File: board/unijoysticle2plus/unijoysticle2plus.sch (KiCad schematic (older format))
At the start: 43 parts, among them J1 DB9_Female, J2 DB9_Female, J3 USB_B_Micro, Q1 S8050, Q2 S8050, SW1 RESET, SW2 JOY SWAP, U1 74HC05, U2 74HC05, U3 74HC05, U4 ESP32-WROOM-32D, U5 AMS1117-3.3, U6 CH340C

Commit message: unijoysticle2plus: no idea
Unfortunately I have no idea what these changes are.
I would guess it is "safe" to commit them.
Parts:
- removed H1, H2: MountingHole_Pad, MountingHole:MountingHole_3.2mm_M3_Pad_Via, symbol Mechanical:MountingHole_Pad
- R2, R3, R4: value 300 -> 1k; LCSC C17617 -> C17513
- renumbered H3 to H1, H4 to H2
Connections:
- wire segments 189 -> 187
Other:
- moved on the sheet: H1, H2
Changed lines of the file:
@@
 	3050 450  3050 3950
-Wire Notes Line
-	6850 4750 6800 4750
 Wire Notes Line
 	3700 5500 11050 5500
@@
 P 6550 5750
 F 0 "R2" V 6620 5750 50  0000 C CNN
-F 1 "300" V 6460 5750 50  0000 C CNN
+F 1 "1k" V 6460 5750 50  0000 C CNN
 F 2 "Resistor_SMD:R_0805_2012Metric_Pad1.20x1.40mm_HandSolder" V 6480 5750 50  0001 C CNN
 F 3 "~" H 6550 5750 50  0001 C CNN
-F 4 "C17617" V 6550 5750 50  0001 C CNN "LCSC"
+F 4 "C17513" V 6550 5750 50  0001 C CNN "LCSC"
 	1    6550 5750
 	0    -1   -1   0
@@
 NoConn ~ 9460 6110
 $Comp
-L Mechanical:MountingHole_Pad H3
-U 1 1 60D40B18
-P 8300 5830
-F 0 "H3" H 8250 6000 50  0000 L CNN
-F 1 "MountingHole_Pad" H 7960 5650 50  0001 L CNN
-F 2 "MountingHole:MountingHole_3.2mm_M3_Pad_Via" H 8300 5830 50  0001 C CNN
-F 3 "~" H 8300 5830 50  0001 C CNN
-	1    8300 5830
-	1    0    0    -1
-$EndComp
-$Comp
-L Mechanical:MountingHole_Pad H4
-U 1 1 60D4139A
-P 8550 5830
-F 0 "H4" H 8500 6000 50  0000 L CNN
-F 1 "MountingHole_Pad" H 8200 5650 50  0001 L CNN
-F 2 "MountingHole:MountingHole_3.2mm_M3_Pad_Via" H 8550 5830 50  0001 C CNN
-F 3 "~" H 8550 5830 50  0001 C CNN
-	1    8550 5830
-	1    0    0    -1
-$EndComp
-$Comp
 L Graphic:Logo_Open_Hardware_Small #LOGO1
 U 1 1 60C7EEFF
@@
 P 6550 6000
 F 0 "R3" V 6620 6000 50  0000 C CNN
-F 1 "300" V 6460 6000 50  0000 C CNN
+F 1 "1k" V 6460 6000 50  0000 C CNN
 F 2 "Resistor_SMD:R_0805_2012Metric_Pad1.20x1.40mm_HandSolder" V 6480 6000 50  0001 C CNN
 F 3 "~" H 6550 6000 50  0001 C CNN
-F 4 "C17617" V 6550 6000 50  0001 C CNN "LCSC"
+F 4 "C17513" V 6550 6000 50  0001 C CNN "LCSC"
 	1    6550 6000
 	0    -1   -1   0
@@
 Text Notes 9120 6310 0    50   ~ 0
 Available GPIOs for future use.\nGPIOs 34-39 are Input only
-$Comp
-L Mechanical:MountingHole_Pad H1
-U 1 1 60D3FB9A
-P 7800 5830
-F 0 "H1" H 7750 6000 50  0000 L CNN
-F 1 "MountingHole_Pad" H 7460 5640 50  0001 L CNN
-F 2 "MountingHole:MountingHole_3.2mm_M3_Pad_Via" H 7800 5830 50  0001 C CNN
-F 3 "~" H 7800 5830 50  0001 C CNN
-	1    7800 5830
-	1    0    0    -1
-$EndComp
 Wire Wire Line
 	4100 1550 3550 1550
@@
 Text Label 10240 3140 0    50   ~ 0
 RTS_PROG
-$Comp
-L Mechanical:MountingHole_Pad H2
-U 1 1 60D4032A
-P 8050 5830
-F 0 "H2" H 8000 6000 50  0000 L CNN
-F 1 "MountingHole_Pad" H 7710 5640 50  0001 L CNN
-F 2 "MountingHole:MountingHole_3.2mm_M3_Pad_Via" H 8050 5830 50  0001 C CNN
-F 3 "~" H 8050 5830 50  0001 C CNN
-	1    8050 5830
-	1    0    0    -1
-$EndComp
-Wire Wire Line
-	8550 5930 8300 5930
-Wire Wire Line
-	8300 5930 8050 5930
-Connection ~ 8300 5930
-Wire Wire Line
-	8050 5930 7800 5930
-Connection ~ 8050 5930
+Wire Wire Line
+	8000 5930 7800 5930
+Connection ~ 7800 5930
 Wire Wire Line
 	7800 5930 7800 6010
-Connection ~ 7800 5930
 $Comp
 L power:GND #PWR0104
@@
 U 1 1 61160901
 P 10180 2440
-F 0 "R8" V 10240 2440 50  0000 C CNN
-F 1 "1K" V 10300 2440 50  0000 C CNN
+F 0 "R8" V 10250 2440 50  0000 C CNN
+F 1 "1K" V 10310 2440 50  0000 C CNN
 F 2 "Resistor_SMD:R_0805_2012Metric_Pad1.20x1.40mm_HandSolder" H 10180 2440 50  0001 C CNN
 F 3 "~" H 10180 2440 50  0001 C CNN
@@
 Wire Wire Line
 	10280 2440 10620 2440
+Wire Wire Line
+	7430 2450 7860 2450
+Wire Wire Line
+	7430 2350 7860 2350
+Wire Wire Line
+	7430 2150 7810 2150
+NoConn ~ 9210 2440
+$Comp
+L Mechanical:MountingHole_Pad H2
+U 1 1 60D4139A
+P 8000 5830
+F 0 "H2" H 7950 6000 50  0000 L CNN
+F 1 "MountingHole_Pad" H 7650 5650 50  0001 L CNN
+F 2 "MountingHole:MountingHole_3.2mm_M3_Pad_Via" H 8000 5830 50  0001 C CNN
+F 3 "~" H 8000 5830 50  0001 C CNN
+	1    8000 5830
+	1    0    0    -1
+$EndComp
+$Comp
+L Mechanical:MountingHole_Pad H1
+U 1 1 60D40B18
+P 7800 5830
+F 0 "H1" H 7750 6000 50  0000 L CNN
+F 1 "MountingHole_Pad" H 7460 5650 50  0001 L CNN
+F 2 "MountingHole:MountingHole_3.2mm_M3_Pad_Via" H 7800 5830 50  0001 C CNN
+F 3 "~" H 7800 5830 50  0001 C CNN
+	1    7800 5830
+	1    0    0    -1
+$EndComp
 $Comp
 L Device:R R4
@@
 P 6550 6250
 F 0 "R4" V 6620 6250 50  0000 C CNN
-F 1 "300" V 6460 6250 50  0000 C CNN
+F 1 "1k" V 6460 6250 50  0000 C CNN
 F 2 "Resistor_SMD:R_0805_2012Metric_Pad1.20x1.40mm_HandSolder" V 6480 6250 50  0001 C CNN
 F 3 "~" H 6550 6250 50  0001 C CNN
-F 4 "C17617" V 6550 6250 50  0001 C CNN "LCSC"
+F 4 "C17513" V 6550 6250 50  0001 C CNN "LCSC"
 	1    6550 6250
 	0    -1   -1   0
 $EndComp
-Wire Wire Line
-	7430 2450 7860 2450
-Wire Wire Line
-	7430 2350 7860 2350
-Wire Wire Line
-	7430 2150 7810 2150
-NoConn ~ 9210 2440
 $EndSCHEMATC

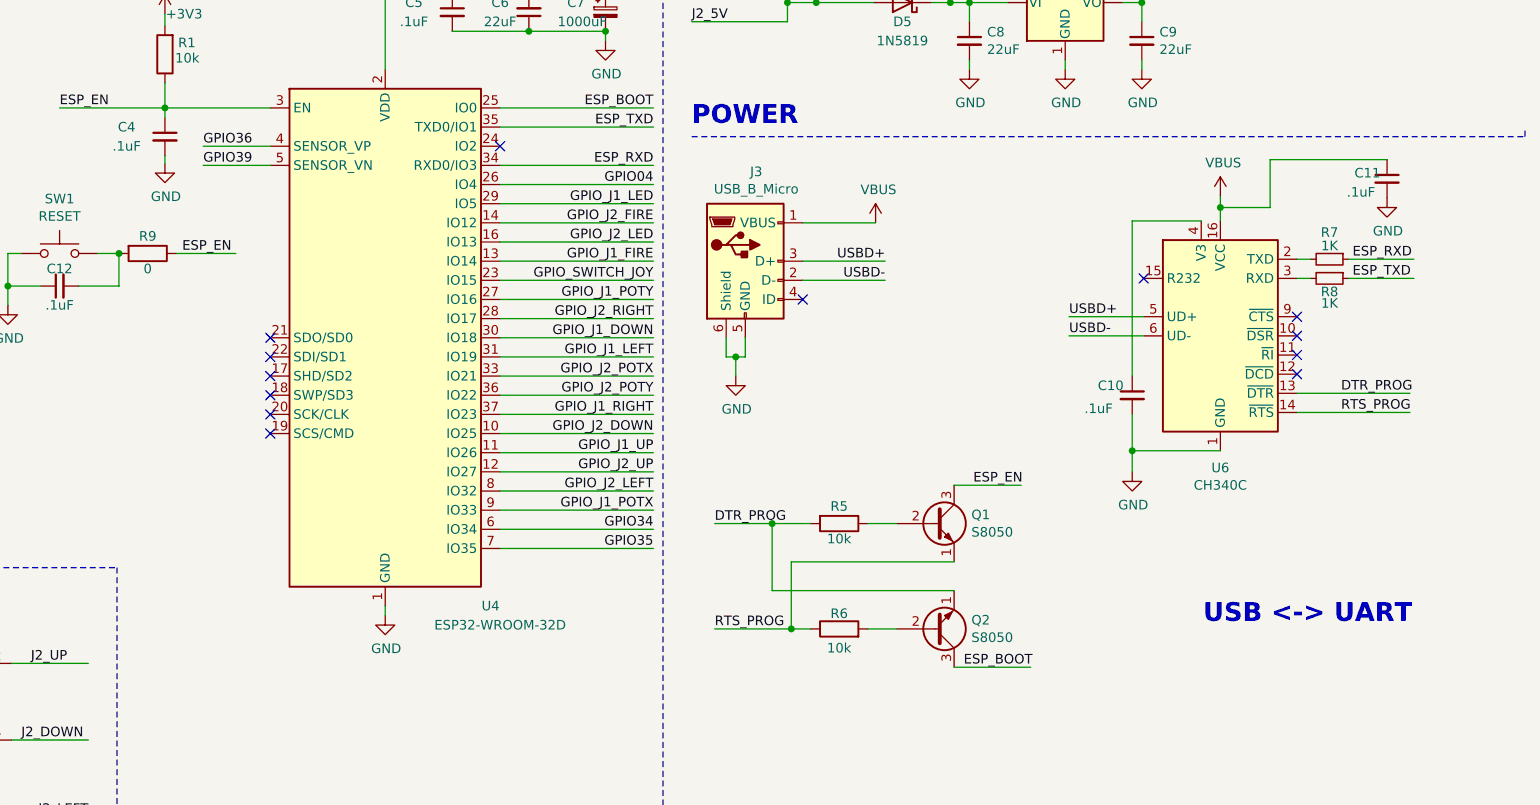
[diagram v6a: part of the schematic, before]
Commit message: unijoysticle2+: rev C WIP
- 5819 package: using SMA instead of SOD-123:
    - I thought the diode was fauly or something... so I dediced to
      change for another one. But I think the bug is somewhere else.
      In any case, using the new part (with different package)
- CH340C: powered using v3.3 instead of v5.
    - ESP EN should be high (v3.3) or low (0), but if CH340 is powered
      using v5, then DTR might have ~4V... instead of v3.3
- Using one MUN5214D insetad of two S8050 + resistors
    - less space, less routing, cheaper... although might not be as easy
      to solder as the S8050
- Using only one power place: removed VBUS and C64-5V power planes.
    - The only power plane is the v3.3+ one
- Layout changed a bit to based on the new components.
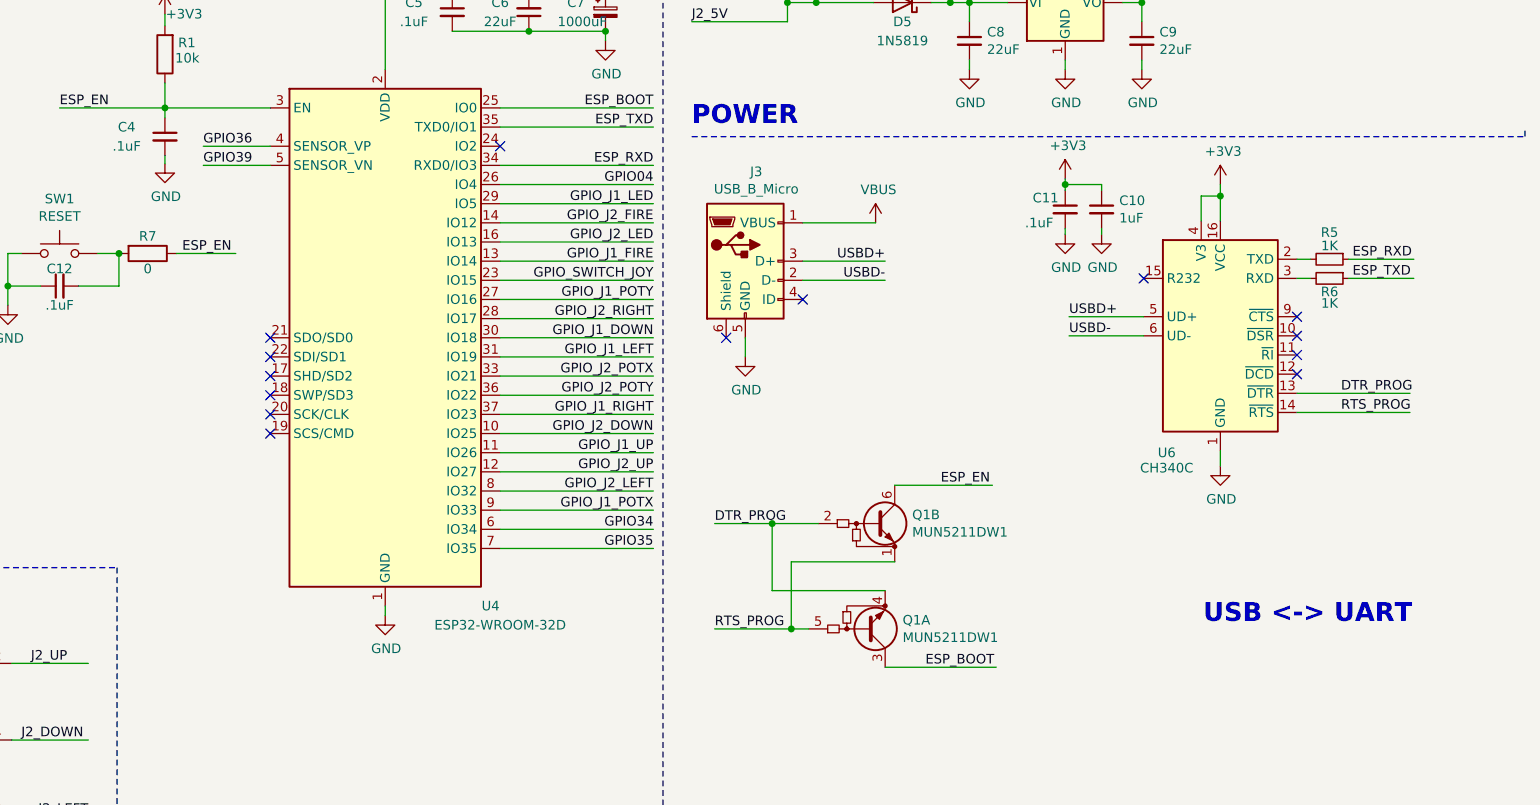
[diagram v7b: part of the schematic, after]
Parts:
- removed Q1, Q2: S8050, Package_TO_SOT_SMD:SOT-23, symbol Transistor_BJT:S8050
- removed R5, R6: 10k, Resistor_SMD:R_0805_2012Metric_Pad1.20x1.40mm_HandSolder, symbol Device:R
- added Q1: MUN5211DW1, Package_TO_SOT_SMD:SOT-363_SC-70-6, symbol Transistor_BJT:MUN5211DW1
- C10: value .1uF -> 1uF; LCSC C28323 -> (none)
- D4, D5: footprint Diode_SMD:D_SOD-123 -> Diode_SMD:D_SMA; LCSC C8598 -> C2480
- renumbered R7 to R5, R8 to R6, R9 to R7
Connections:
- wire segments 187 -> 182
- no-connect marks 18 -> 19
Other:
- moved on the sheet: C11

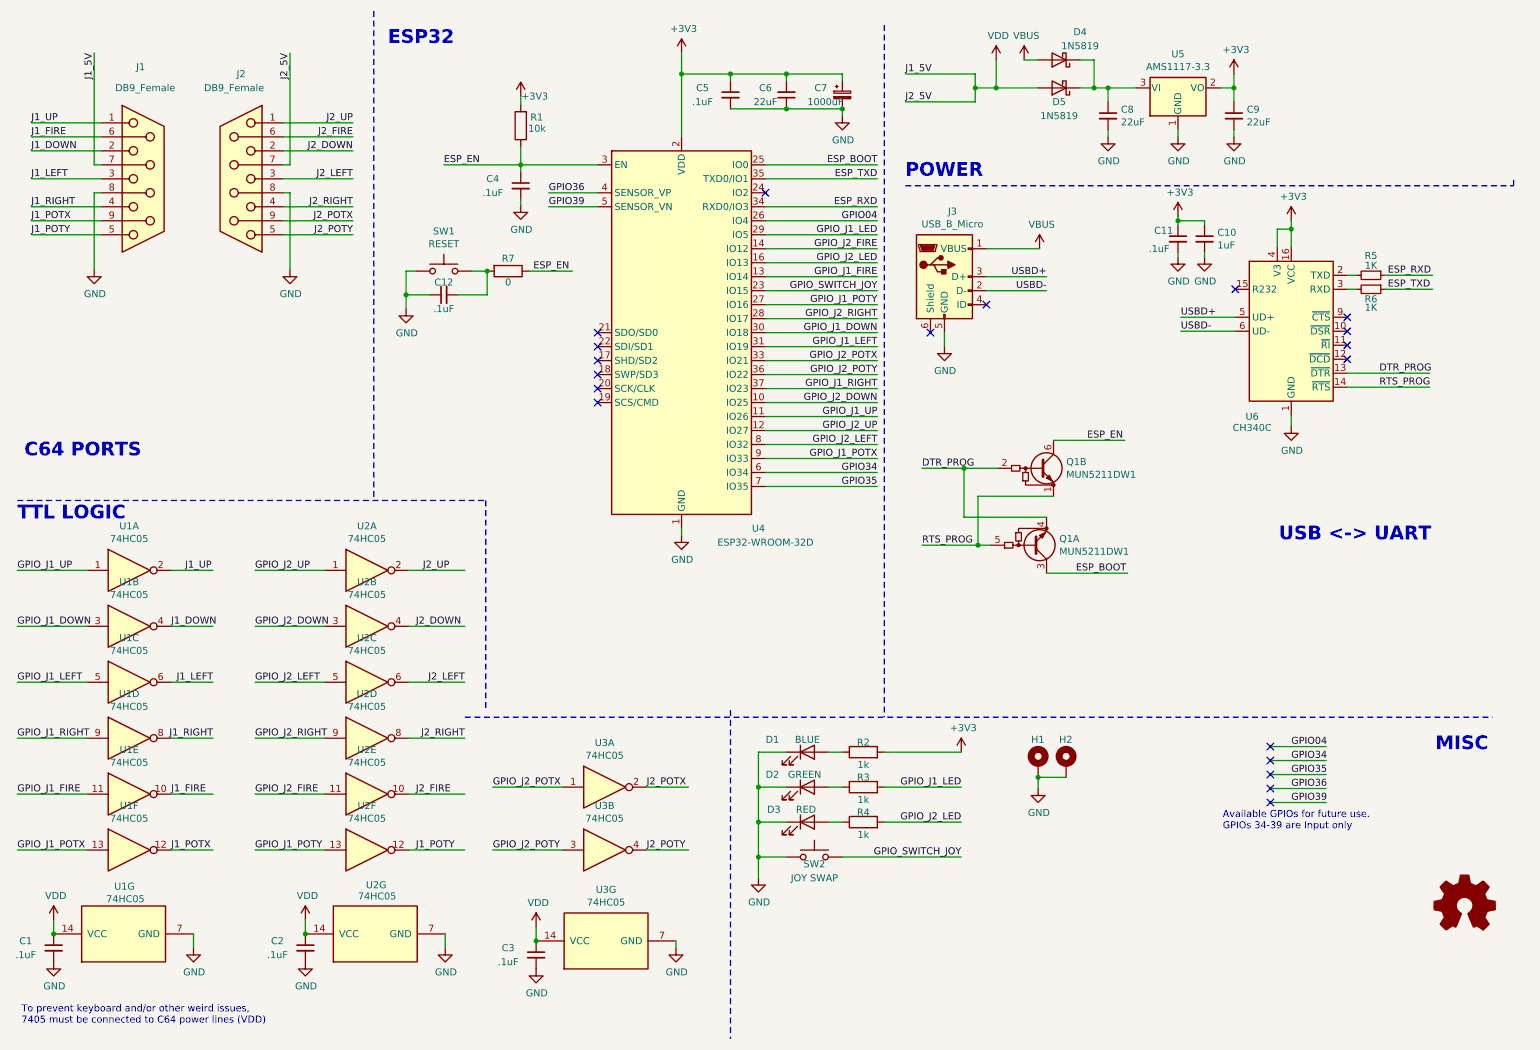
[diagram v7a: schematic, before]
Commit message: unijoysticle2plus: boot button and more
- Remove power plane. Plane #2 and #3 are GND planes now
- Add Boot button, easier to debug should we need it
- New USB Micro B package + footprint
- Renamed VDD with +5V
- Added PWR_FLAG for +5v to prevent warnings
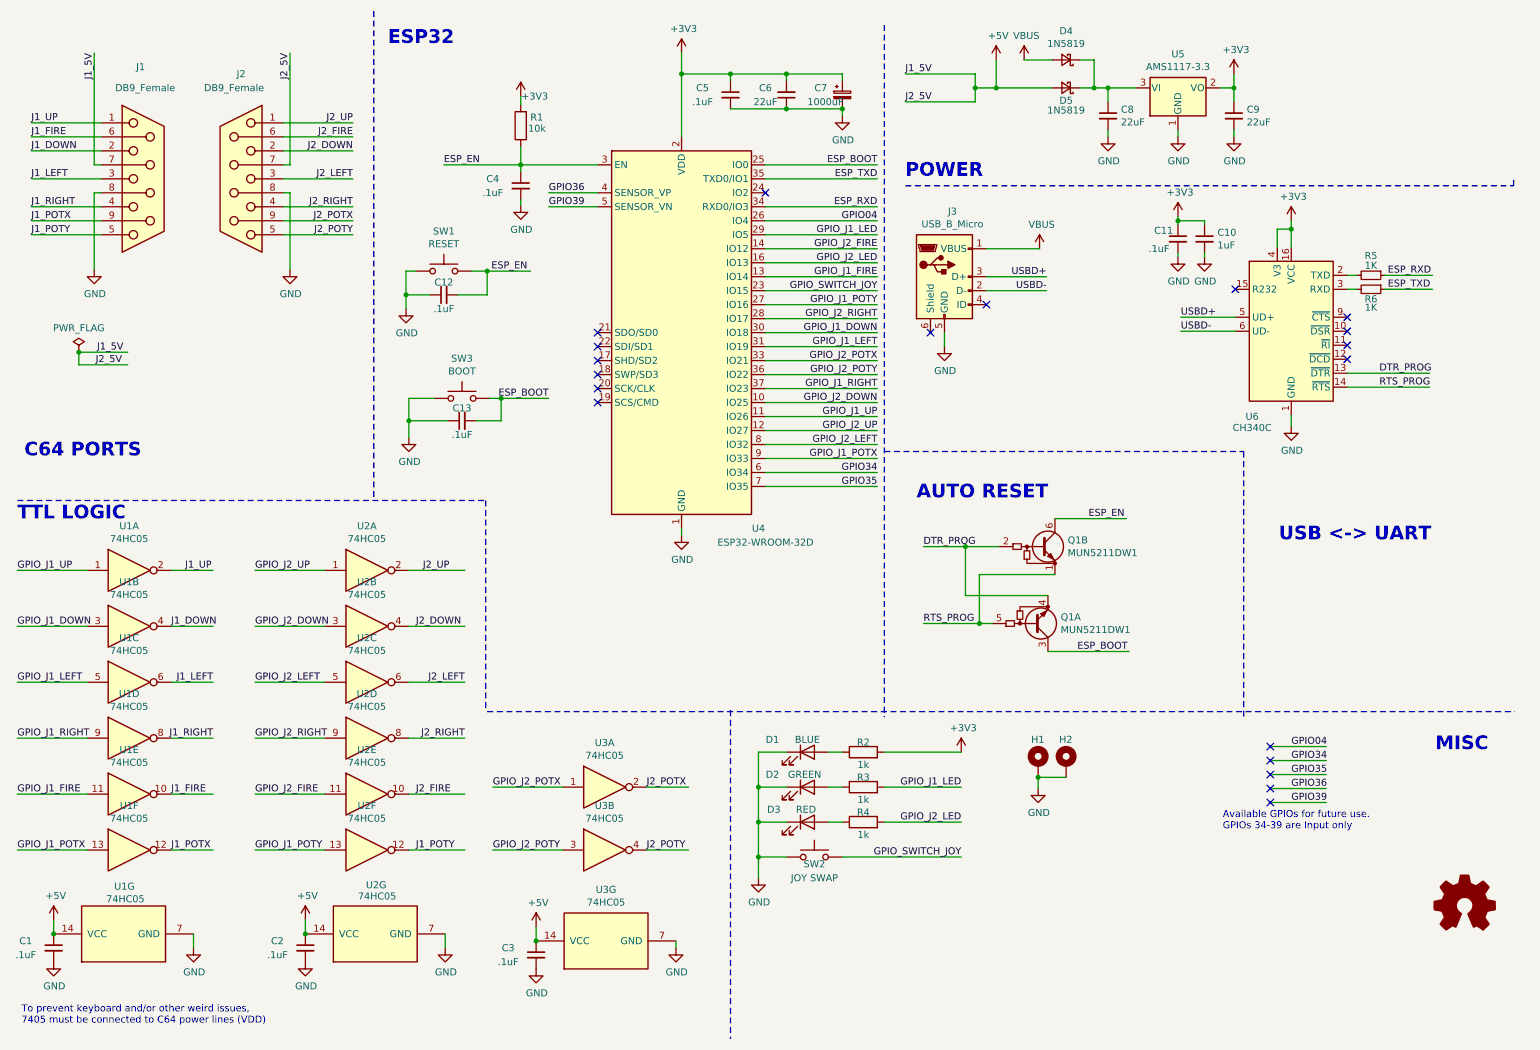
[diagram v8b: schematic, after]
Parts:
- removed D4, D5: 1N5819, Diode_SMD:D_SMA, symbol Diode:1N5819
- removed R7: 0, Resistor_SMD:R_0805_2012Metric_Pad1.20x1.40mm_HandSolder, symbol Device:R
- added C13: .1uF, Capacitor_SMD:C_0805_2012Metric_Pad1.18x1.45mm_HandSolder, symbol Device:C_Small
- added D4, D5: 1N5819, Diode_SMD:D_SMA, symbol Device:D_Schottky_Small
- added SW3: BOOT, Unijoysticle:SW_Push_1P1T_NO_5.1x5.1mm, symbol Switch:SW_Push
- J3: footprint Connector_USB:USB_Micro-B_Molex_47346-0001 -> Unijoysticle:MicroXNJ; LCSC C132560 -> C404969
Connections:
- net labels added: +5V
- net labels removed: VDD
- wire segments 182 -> 193
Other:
- note added: "AUTO RESET"
- moved on the sheet: Q1A, Q1B
